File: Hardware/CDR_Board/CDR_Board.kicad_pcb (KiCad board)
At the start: 2 copper layers, 61 x 40.6 mm, 62 parts, among them J1 nRF52, J2 nRF24, J3 Battery, J4 GPIO & ADC, J5 USB_C_Receptacle_USB2.0, Q1 DMP2045U, SW1 BOOTSEL, SW2 RESET, SW3 SW_SPDT, U1 W25Q32JVSS, U2 AP2112, U3 RP2040, U4 BQ25172, U6 ADXL343, Y1 Crystal

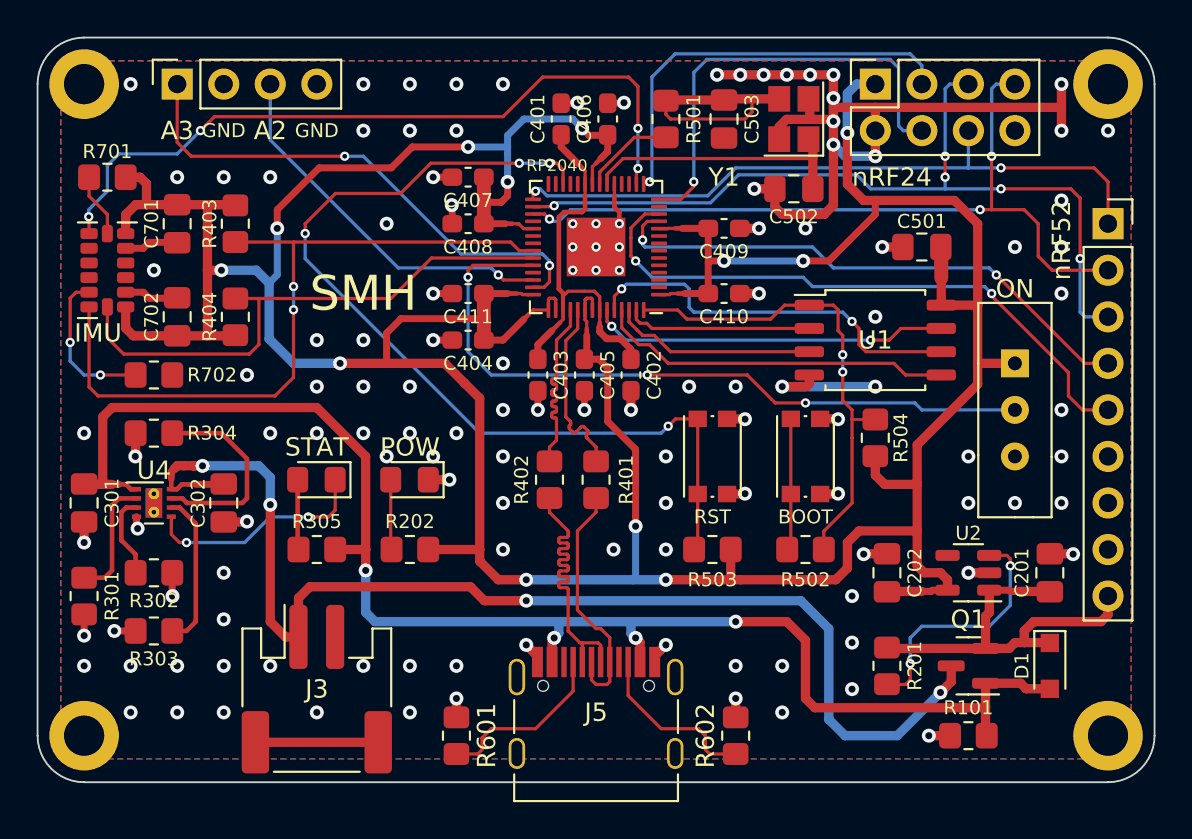
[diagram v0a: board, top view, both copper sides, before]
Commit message: Updated helmet PCB
Added voltage divider for battery measurement, pull-down resistor for FSR measurement
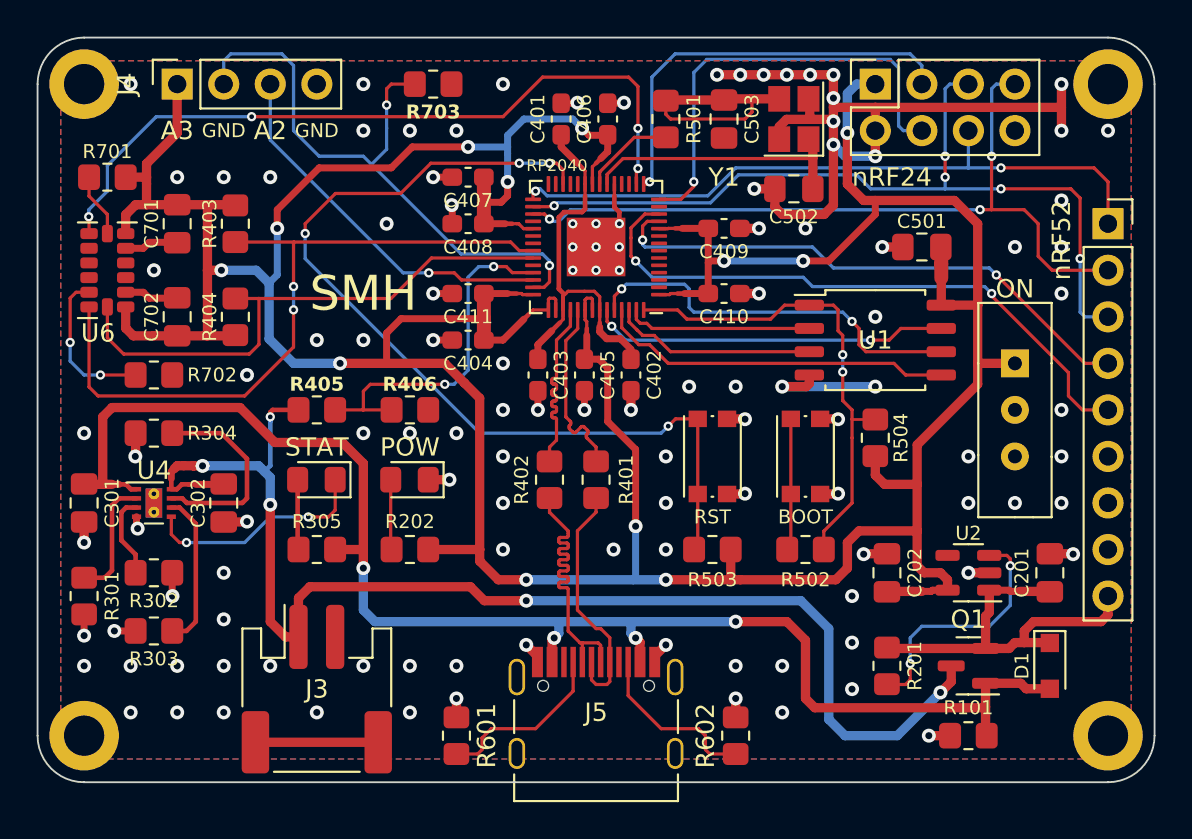
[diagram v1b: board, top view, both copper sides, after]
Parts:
- added R405: 10K, Resistor_SMD:R_0805_2012Metric_Pad1.20x1.40mm_HandSolder, F.Cu at (137.2, 96.5)
- added R406: 10K, Resistor_SMD:R_0805_2012Metric_Pad1.20x1.40mm_HandSolder, F.Cu at (142.2, 96.5)
- added R703: 10k, Resistor_SMD:R_0805_2012Metric_Pad1.20x1.40mm_HandSolder, F.Cu at (143.5, 78.7)
- J4: value GPIO & ADC -> Conn_01x04
- U6: value ADXL343 -> ADXL375
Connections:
- J4 pad 1: /A3 -> +3V3
- J4 pad 2: GND -> /A3
- SW3 pad 2: /A0 -> unconnected-(SW3-B-Pad2)
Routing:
- net /A0: track 39.3 -> 0.00 mm, vias 3 -> 0
- net /A1: track 0.00 -> 19.3 mm, vias 0 -> 2
- net +3V3: track 228.6 -> 234.6 mm
- net /A3: track 28.3 -> 34.3 mm
- net +BATT: track 65.8 -> 70.8 mm, vias 4 -> 5
- net /SDA: track 40.0 -> 39.0 mm
- net GND: vias 128 -> 119
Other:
- board text added: "SDP23 Team 31: Helmet Board v1.2 JLCJLCJLCJLC A. Sahay, M. Morel, M.P. Gonzalez, R. Patel Prof. Arbabi"
- board text added: "U6"
- board text removed: "IMU"
- board text removed: "SDP23 Team 31: Helmet Board v1 JLCJLCJLCJLC A. Sahay, M. Morel, M.P. Gonzalez, R. Patel Prof. Arbabi"

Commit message: Updated ADXL375 I2C, helmet PCB
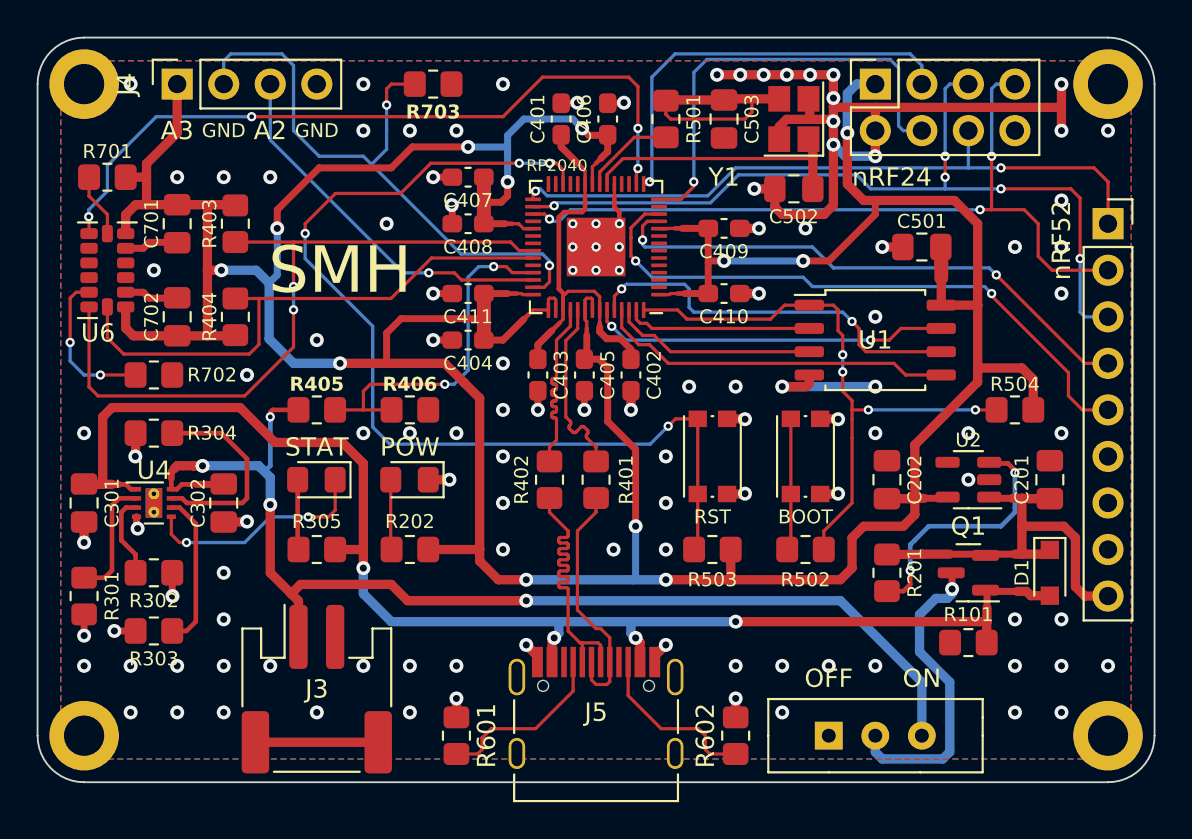
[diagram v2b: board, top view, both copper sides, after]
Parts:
- SW3: value SW_SPDT -> POW_ON
- moved SW3 22.7 mm to (165.1, 114.3), turned to 90 degrees
- moved R504 7.77 mm to (175.3, 96.5), turned to 180 degrees
- moved C201 5.08 mm to (177.2, 100.3)
- moved C202 5.08 mm to (168.3, 100.3)
- moved D1 5.08 mm to (177.2, 105.4)
- moved Q1 5.08 mm to (172.7, 105.4)
- moved R101 5.08 mm to (172.7, 109.2)
- moved R201 5.08 mm to (168.3, 105.4)
- moved U2 5.08 mm to (172.7, 100.3)
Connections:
- net /D13 renamed /ACC_INT1
- net Net-(C503-Pad2) renamed /XOUT_R
- net Net-(J5-CC1) renamed /CC1
- net Net-(J5-CC2) renamed /CC2
- net Net-(U1-DI(IO0)) renamed /QSPI_SD0
- net Net-(U1-DO(IO1)) renamed /QSPI_SD1
- net Net-(U1-IO2) renamed /QSPI_SD2
- net Net-(U1-IO3) renamed /QSPI_SD3
- net Net-(U4-ISET) renamed /ISET
- net Net-(U4-TMR) renamed /TMR
- net Net-(U4-TS) renamed /TS
- net Net-(U4-VSET) renamed /VSET
- net Net-(U6-SDO/ADDR) renamed /ACC_ADDR
- net Net-(U6-~{CS}) renamed /ACC_CS
- C302 pad 1: +BATT -> /+B_IN
- J3 pad 1: +BATT -> /+B_IN
- R405 pad 1: +BATT -> /+B_IN
- SW3 pad 1: +3V3 -> GND
- SW3 pad 2: unconnected-(SW3-B-Pad2) -> +BATT
- SW3 pad 3: GND -> /+B_IN
- U4 pad 8: +BATT -> /+B_IN
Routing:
- net /+B_IN: track 0.00 -> 63.8 mm, vias 0 -> 4
- net +BATT: track 70.8 -> 16.9 mm, vias 5 -> 1
- net /FLASH_CS: track 26.1 -> 32.7 mm, vias 2 -> 4
- net +3V3: track 234.6 -> 229.1 mm
- net GND: track 94.7 -> 89.9 mm, vias 119 -> 118
- net VBUS: track 81.8 -> 77.5 mm
- net /RUN: track 51.2 -> 54.9 mm
- net /VSRC: track 22.3 -> 23.3 mm
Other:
- board text added: "OFF"
